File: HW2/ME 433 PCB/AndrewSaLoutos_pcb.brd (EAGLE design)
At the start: 50 x 50 mm, 23 parts

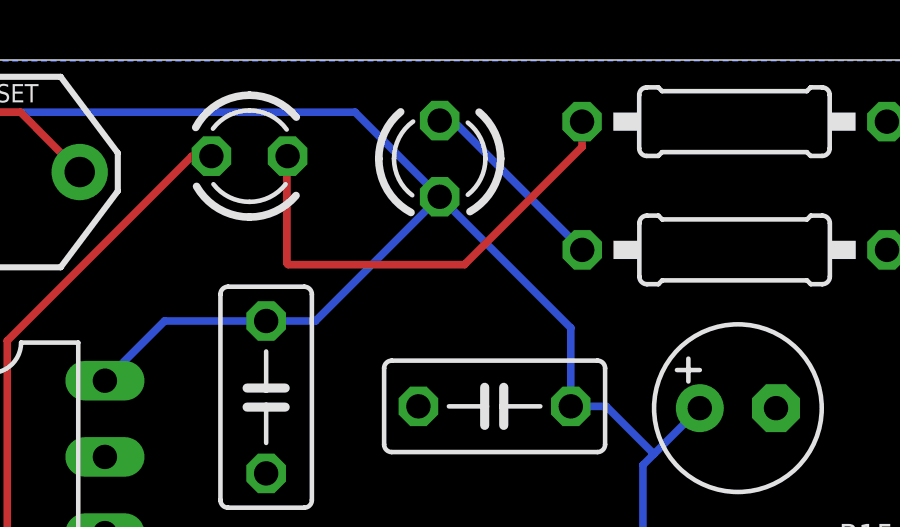
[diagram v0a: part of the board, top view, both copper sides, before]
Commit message: Rotated LED
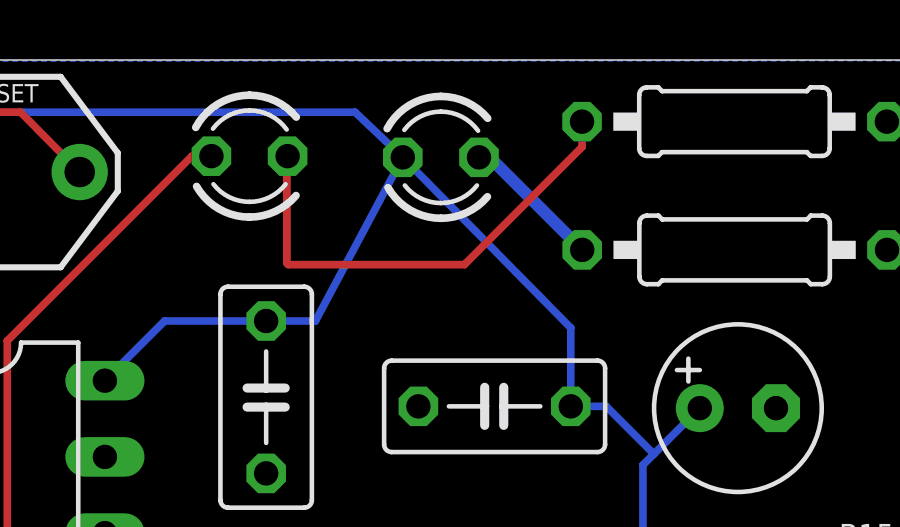
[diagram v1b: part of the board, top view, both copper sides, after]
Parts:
- moved LED2 0.06 mm to (32.2, 46.8), turned to 0 degrees
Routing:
- net N$17: track 6.54 -> 4.72 mm
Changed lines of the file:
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@@
 <attribute name="VALUE" x="23.485" y="42.969" size="1.27" layer="27" ratio="10"/>
 </element>
-<element name="LED2" library="433_lib" package="LED3MM" value="Red" x="32.195" y="46.71" smashed="yes" rot="R90">
-<attribute name="VALUE" x="33.621" y="44.315" size="1.27" layer="27" ratio="10" rot="R180"/>
+<element name="LED2" library="433_lib" package="LED3MM" value="Red" x="32.235" y="46.755" smashed="yes">
+<attribute name="VALUE" x="33.54" y="44.229" size="1.27" layer="27" ratio="10" rot="R180"/>
 </element>
 <element name="R1" library="433_lib" package="0207/10" value="10k" x="5.37" y="34.795" smashed="yes" rot="R90">
@@
 <wire x1="37.745" y1="38.455" x2="39.335" y2="36.865" width="0.254" layer="16"/>
 <wire x1="36.565" y1="38.455" x2="36.565" y2="41.07" width="0.254" layer="16"/>
-<wire x1="32.195" y1="45.44" x2="36.565" y2="41.07" width="0.254" layer="16"/>
+<wire x1="30.965" y1="46.755" x2="36.565" y2="41.07" width="0.254" layer="16"/>
 <wire x1="28.055" y1="41.3" x2="26.41" y2="41.3" width="0.254" layer="16"/>
-<wire x1="28.055" y1="41.3" x2="32.195" y2="45.44" width="0.254" layer="16"/>
+<wire x1="28.055" y1="41.3" x2="30.965" y2="46.755" width="0.254" layer="16"/>
 <wire x1="26.41" y1="41.3" x2="23.025" y2="41.3" width="0.254" layer="16"/>
 <wire x1="23.025" y1="41.3" x2="21.035" y2="39.31" width="0.254" layer="16"/>
@@
 <wire x1="1.27" y1="44.45" x2="5.08" y2="48.26" width="0.254" layer="16"/>
 <wire x1="5.08" y1="48.26" x2="29.375" y2="48.26" width="0.254" layer="16"/>
-<wire x1="29.375" y1="48.26" x2="32.195" y2="45.44" width="0.254" layer="16"/>
+<wire x1="29.375" y1="48.26" x2="30.965" y2="46.755" width="0.254" layer="16"/>
 </signal>
 <signal name="N$1">
@@
 <contactref element="R4" pad="2"/>
 <contactref element="LED2" pad="K"/>
-<wire x1="32.195" y1="47.98" x2="32.635" y2="47.98" width="0.254" layer="16"/>
-<wire x1="32.635" y1="47.98" x2="36.945" y2="43.67" width="0.254" layer="16"/>
+<wire x1="33.505" y1="46.755" x2="33.86" y2="46.755" width="0.4064" layer="16"/>
+<wire x1="33.86" y1="46.755" x2="36.945" y2="43.67" width="0.4064" layer="16"/>
 </signal>
 <signal name="USBID">
